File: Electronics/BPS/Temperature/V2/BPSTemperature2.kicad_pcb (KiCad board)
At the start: 2 copper layers, 75 x 65 mm, 80 parts, among them J1 Conn_02x10_Counter_Clockwise, J2 Logic Analyzer, J3 Conn_02x06_Counter_Clockwise, J4 Conn_02x06_Counter_Clockwise, SW1 SW_DIP_x06, U1 LTC2983

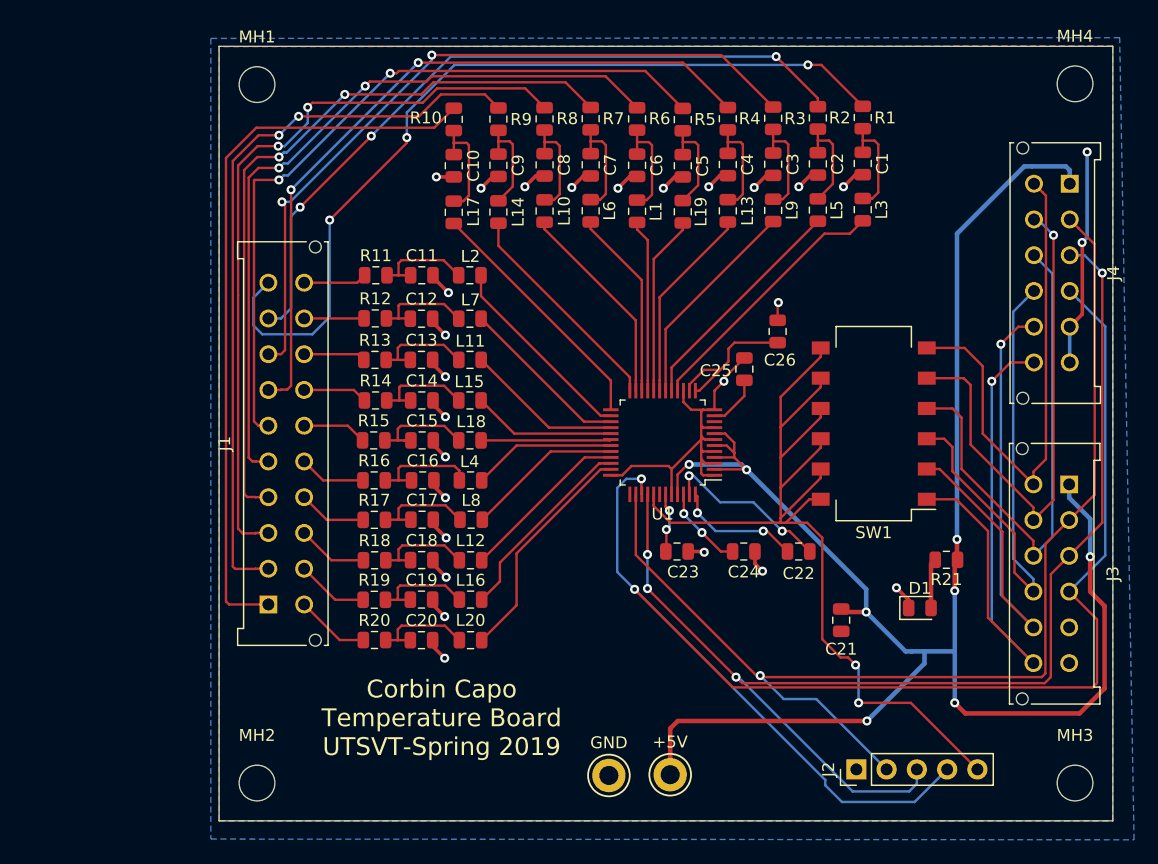
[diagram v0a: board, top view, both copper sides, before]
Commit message: Rotated components of Temperature Board for BPS
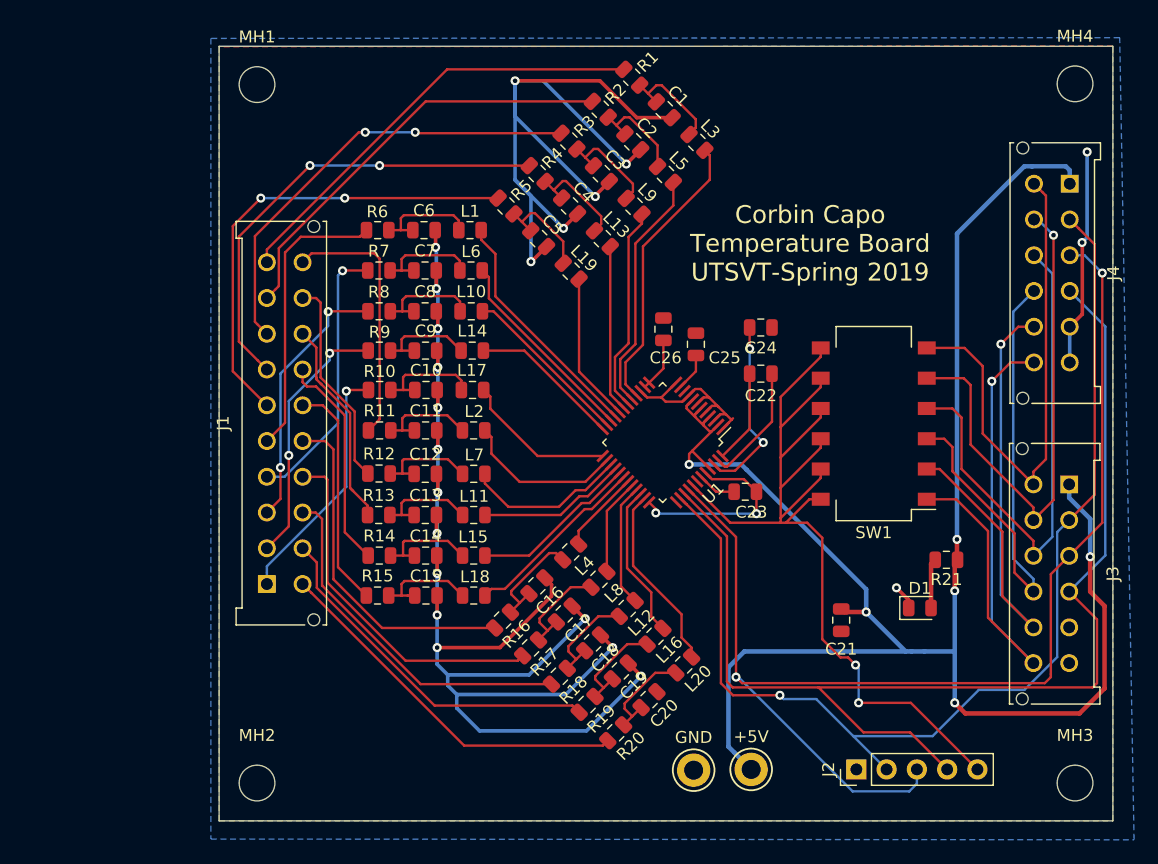
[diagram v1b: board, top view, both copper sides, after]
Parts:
- moved R6 23.7 mm to (73.3, 85.4), turned to 0 degrees
- moved R10 23.5 mm to (73.5, 98.8), turned to 0 degrees
- moved R7 21.9 mm to (73.4, 88.8), turned to 0 degrees
- moved R9 21.8 mm to (73.4, 95.5), turned to 0 degrees
- moved R20 21.7 mm to (93.3, 127.6), turned to 45 degrees
- moved R8 21.3 mm to (73.4, 92.2), turned to 0 degrees
- moved R19 19.9 mm to (90.9, 125.2), turned to 45 degrees
- moved C20 19.7 mm to (96.1, 124.8), turned to 45 degrees
- moved R1 19.7 mm to (94.6, 72.6), turned to 315 degrees
- moved C10 19.0 mm to (77.4, 98.8), turned to 0 degrees
- moved C24 18.9 mm to (105.5, 93.6)
- moved C6 18.7 mm to (77.2, 85.4), turned to 0 degrees
- moved R18 18.3 mm to (88.6, 122.9), turned to 45 degrees
- moved R2 18.3 mm to (92.0, 75.3), turned to 315 degrees
- moved L20 18.0 mm to (99.0, 121.9), turned to 225 degrees
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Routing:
- net GND: track 95.2 -> 239.7 mm, vias 27 -> 24
- net /CH10_LPF: track 61.7 -> 20.9 mm, vias 0 -> 1
- net /CH8_LPF: track 63.0 -> 22.3 mm
- net /CH9_LPF: track 62.2 -> 21.9 mm
- net /CH7_LPF: track 62.3 -> 22.9 mm, vias 2 -> 1
- net /CH6_LPF: track 62.5 -> 24.1 mm, vias 2 -> 0
- net /CH1_LPF: track 72.6 -> 37.3 mm, vias 3 -> 0
- net /MISO: track 126.5 -> 98.6 mm, vias 2 -> 0
- net /CH2_LPF: track 61.9 -> 36.0 mm, vias 3 -> 0
- net /CH20_LPF: track 6.20 -> 31.4 mm
- net /CH3_LPF: track 62.5 -> 37.9 mm
- net /CH17_LPF: track 5.74 -> 30.1 mm
- net /CH18_LPF: track 5.93 -> 30.1 mm
- net /CH19_LPF: track 6.03 -> 30.2 mm
- net /CH16_LPF: track 5.60 -> 29.0 mm
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
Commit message: Modified rotated board for BPS
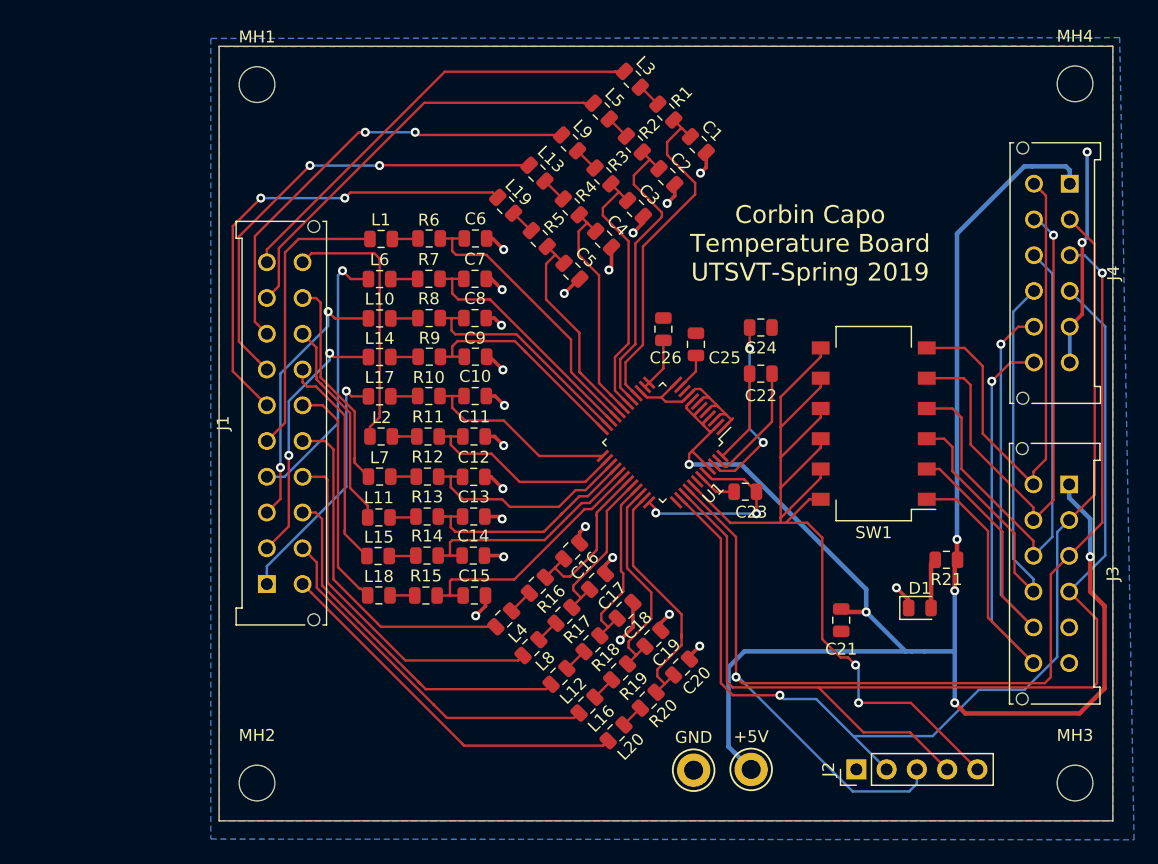
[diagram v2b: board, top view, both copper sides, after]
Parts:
- moved L16 8.12 mm to (90.9, 125.3), turned to 45 degrees
- moved L8 8.09 mm to (86.2, 120.5), turned to 45 degrees
- moved L12 8.08 mm to (88.5, 122.9), turned to 45 degrees
- moved L20 8.04 mm to (93.3, 127.6), turned to 45 degrees
- moved L15 8.02 mm to (73.3, 112.8), turned to 0 degrees
- moved L11 7.97 mm to (73.4, 109.5), turned to 0 degrees
- moved L18 7.96 mm to (73.4, 116.1), turned to 0 degrees
- moved L4 7.94 mm to (83.9, 118.0), turned to 45 degrees
- moved L7 7.90 mm to (73.5, 106.1), turned to 0 degrees
- moved L17 7.82 mm to (73.5, 99.4)
- moved L14 7.79 mm to (73.5, 96.1), turned to 0 degrees
- moved L19 7.79 mm to (84.0, 83.3)
- moved L2 7.78 mm to (73.6, 102.7), turned to 0 degrees
- moved L13 7.77 mm to (86.7, 80.6)
- moved L10 7.71 mm to (73.5, 92.8), turned to 0 degrees
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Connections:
- L1 pad 1: Net-(L1-Pad1) -> /CH6_LPF
- L1 pad 2: Net-(C6-Pad1) -> Net-(L1-Pad2)
- L10 pad 1: Net-(L10-Pad1) -> /CH8_LPF
- L10 pad 2: Net-(C8-Pad1) -> Net-(L10-Pad2)
- L11 pad 1: Net-(L11-Pad1) -> /CH13_LPF
- L11 pad 2: Net-(C13-Pad1) -> Net-(L11-Pad2)
- L12 pad 1: Net-(L12-Pad1) -> /CH18_LPF
- L12 pad 2: Net-(C18-Pad1) -> Net-(L12-Pad2)
- L13 pad 2: Net-(C4-Pad1) -> /CH4_LPF
- L14 pad 1: Net-(L14-Pad1) -> /CH9_LPF
- L14 pad 2: Net-(C9-Pad1) -> Net-(L14-Pad2)
- L15 pad 1: Net-(L15-Pad1) -> /CH14_LPF
- L15 pad 2: Net-(C14-Pad1) -> Net-(L15-Pad2)
- L16 pad 1: Net-(L16-Pad1) -> /CH19_LPF
- L16 pad 2: Net-(C19-Pad1) -> Net-(L16-Pad2)
- L17 pad 2: Net-(C10-Pad1) -> /CH10_LPF
- L18 pad 1: Net-(L18-Pad1) -> /CH15_LPF
- L18 pad 2: Net-(C15-Pad1) -> Net-(L18-Pad2)
- L19 pad 2: Net-(C5-Pad1) -> /CH5_LPF
- L2 pad 1: Net-(L2-Pad1) -> /CH11_LPF
- L2 pad 2: Net-(C11-Pad1) -> Net-(L2-Pad2)
- L20 pad 1: Net-(L20-Pad1) -> /CH20_LPF
- L20 pad 2: Net-(C20-Pad1) -> Net-(L20-Pad2)
- L3 pad 2: Net-(C1-Pad1) -> /CH1_LPF
- L4 pad 1: Net-(L4-Pad1) -> /CH16_LPF
- L4 pad 2: Net-(C16-Pad1) -> Net-(L4-Pad2)
- L5 pad 2: Net-(C2-Pad1) -> /CH2_LPF
- L6 pad 1: Net-(L6-Pad1) -> /CH7_LPF
- L6 pad 2: Net-(C7-Pad1) -> Net-(L6-Pad2)
- L7 pad 1: Net-(L7-Pad1) -> /CH12_LPF
- L7 pad 2: Net-(C12-Pad1) -> Net-(L7-Pad2)
- L8 pad 1: Net-(L8-Pad1) -> /CH17_LPF
- L8 pad 2: Net-(C17-Pad1) -> Net-(L8-Pad2)
- L9 pad 2: Net-(C3-Pad1) -> /CH3_LPF
- R1 pad 1: /CH1_LPF -> Net-(L3-Pad1)
- R10 pad 1: /CH10_LPF -> Net-(L17-Pad1)
- R11 pad 1: /CH11_LPF -> Net-(L2-Pad2)
- R12 pad 1: /CH12_LPF -> Net-(L7-Pad2)
- R13 pad 1: /CH13_LPF -> Net-(L11-Pad2)
- R14 pad 1: /CH14_LPF -> Net-(L15-Pad2)
- R15 pad 1: /CH15_LPF -> Net-(L18-Pad2)
- R16 pad 1: /CH16_LPF -> Net-(L4-Pad2)
- R17 pad 1: /CH17_LPF -> Net-(L8-Pad2)
- R18 pad 1: /CH18_LPF -> Net-(L12-Pad2)
- R19 pad 1: /CH19_LPF -> Net-(L16-Pad2)
- R2 pad 1: /CH2_LPF -> Net-(L5-Pad1)
- R20 pad 1: /CH20_LPF -> Net-(L20-Pad2)
- R3 pad 1: /CH3_LPF -> Net-(L9-Pad1)
- R4 pad 1: /CH4_LPF -> Net-(L13-Pad1)
- R5 pad 1: /CH5_LPF -> Net-(L19-Pad1)
- R6 pad 1: /CH6_LPF -> Net-(L1-Pad2)
- R7 pad 1: /CH7_LPF -> Net-(L6-Pad2)
- R8 pad 1: /CH8_LPF -> Net-(L10-Pad2)
- R9 pad 1: /CH9_LPF -> Net-(L14-Pad2)
- U1 pad 16: Net-(L3-Pad1) -> Net-(C1-Pad1)
- U1 pad 17: Net-(L5-Pad1) -> Net-(C2-Pad1)
- U1 pad 18: Net-(L9-Pad1) -> Net-(C3-Pad1)
- U1 pad 19: Net-(L13-Pad1) -> Net-(C4-Pad1)
- U1 pad 20: Net-(L19-Pad1) -> Net-(C5-Pad1)
- U1 pad 21: Net-(L1-Pad1) -> Net-(C6-Pad1)
- U1 pad 22: Net-(L6-Pad1) -> Net-(C7-Pad1)
- U1 pad 23: Net-(L10-Pad1) -> Net-(C8-Pad1)
- U1 pad 24: Net-(L14-Pad1) -> Net-(C9-Pad1)
- U1 pad 25: Net-(L17-Pad1) -> Net-(C10-Pad1)
- U1 pad 26: Net-(L2-Pad1) -> Net-(C11-Pad1)
- U1 pad 27: Net-(L7-Pad1) -> Net-(C12-Pad1)
- U1 pad 28: Net-(L11-Pad1) -> Net-(C13-Pad1)
- U1 pad 29: Net-(L15-Pad1) -> Net-(C14-Pad1)
- U1 pad 30: Net-(L18-Pad1) -> Net-(C15-Pad1)
- U1 pad 31: Net-(L4-Pad1) -> Net-(C16-Pad1)
- U1 pad 32: Net-(L8-Pad1) -> Net-(C17-Pad1)
- U1 pad 33: Net-(L12-Pad1) -> Net-(C18-Pad1)
- U1 pad 34: Net-(L16-Pad1) -> Net-(C19-Pad1)
- U1 pad 35: Net-(L20-Pad1) -> Net-(C20-Pad1)
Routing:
- net GND: track 239.7 -> 90.1 mm, vias 24 -> 25
- net Net-(L3-Pad1): track 24.0 -> 2.07 mm
- net Net-(L1-Pad1): track 20.3 -> 0.00 mm
- net Net-(C1-Pad1): track 8.97 -> 28.7 mm
- net Net-(L5-Pad1): track 20.5 -> 2.04 mm
- net Net-(L6-Pad1): track 17.1 -> 0.00 mm
- net Net-(C2-Pad1): track 8.47 -> 25.5 mm
- net Net-(L18-Pad1): track 15.8 -> 0.00 mm
- net Net-(L20-Pad1): track 15.8 -> 0.00 mm
- net Net-(L9-Pad1): track 17.3 -> 2.08 mm
- net Net-(C6-Pad1): track 8.97 -> 24.1 mm
- net Net-(L10-Pad1): track 14.4 -> 0.00 mm
- net Net-(L15-Pad1): track 14.2 -> 0.00 mm
- net Net-(L7-Pad1): track 13.7 -> 0.00 mm
- net Net-(L2-Pad1): track 13.6 -> 0.00 mm
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
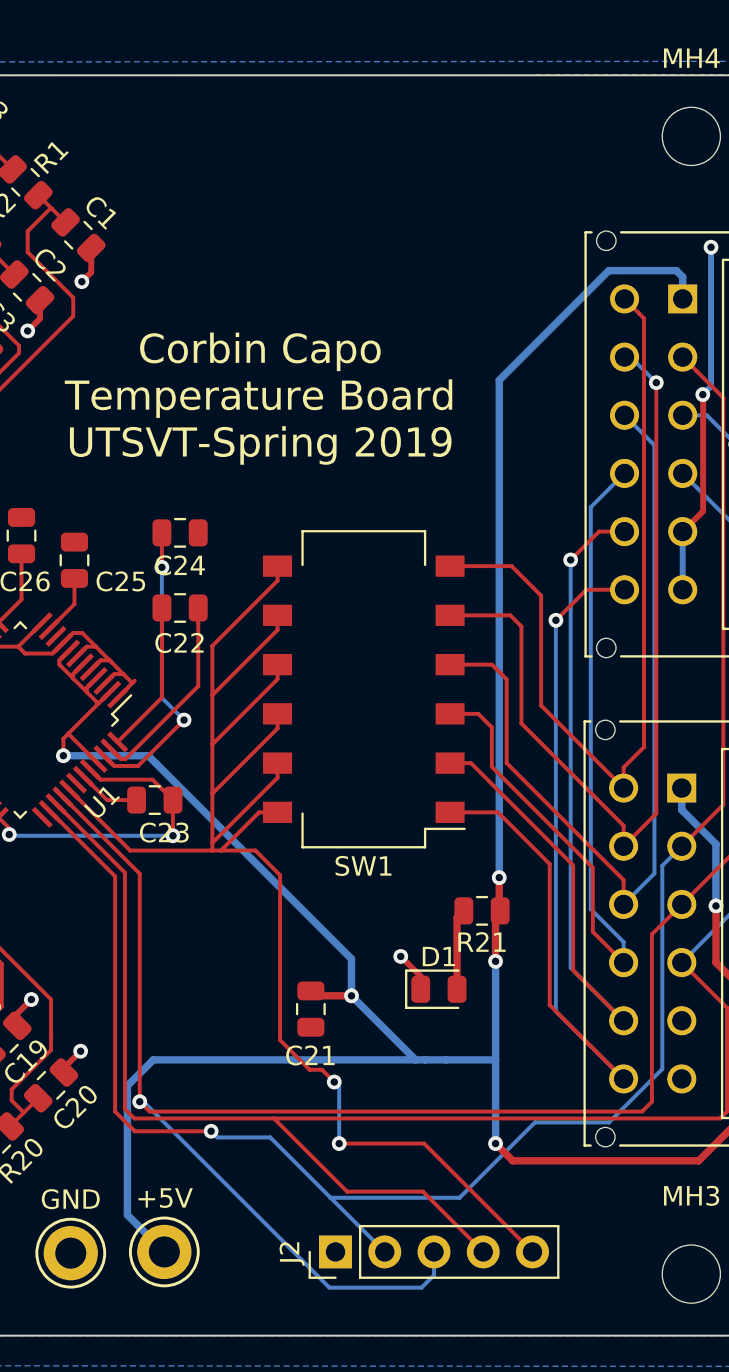
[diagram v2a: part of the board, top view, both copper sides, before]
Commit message: Added connector to temerature board for BPS
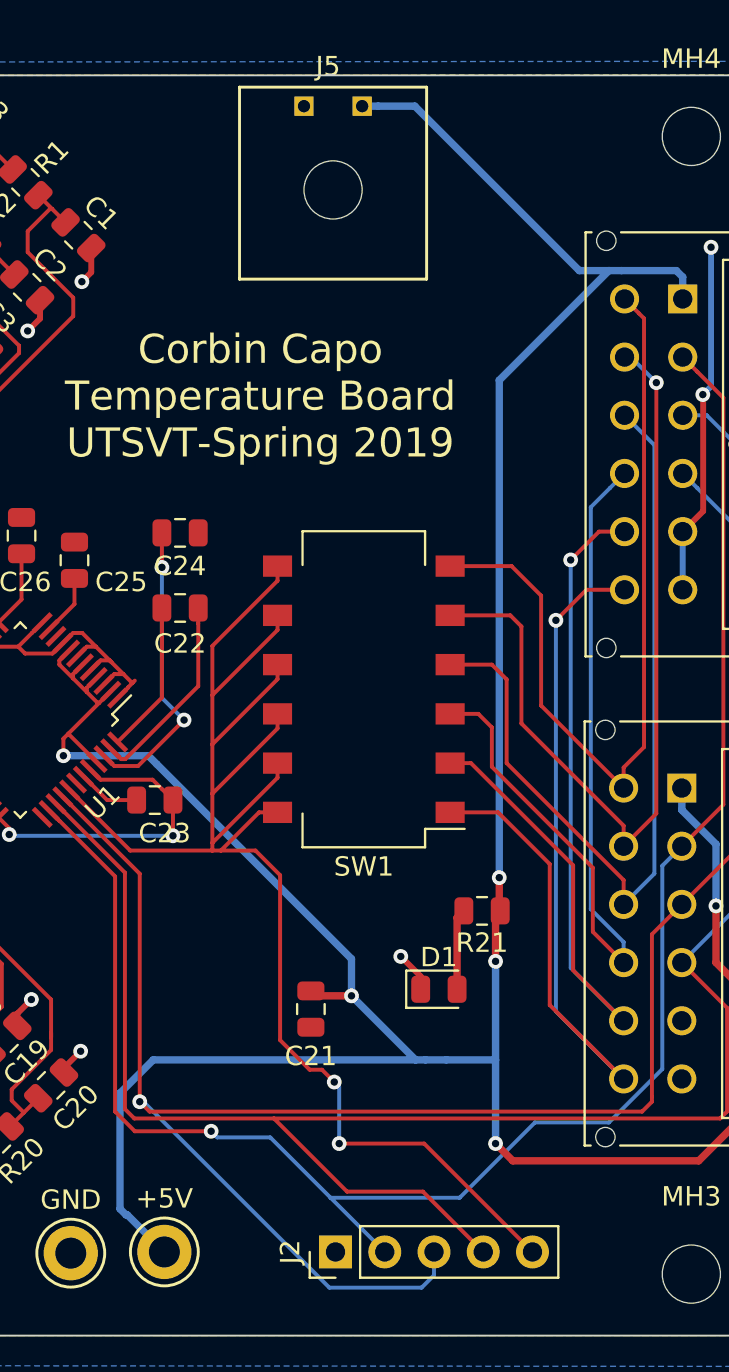
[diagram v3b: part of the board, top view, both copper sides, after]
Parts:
- added J5: Conn_01x02, UTSVT_Connectors:43650-0202_01x02_Microfit 3.0_horizontal, F.Cu at (118.2, 70.6)
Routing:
- net +5V: track 153.9 -> 170.5 mm

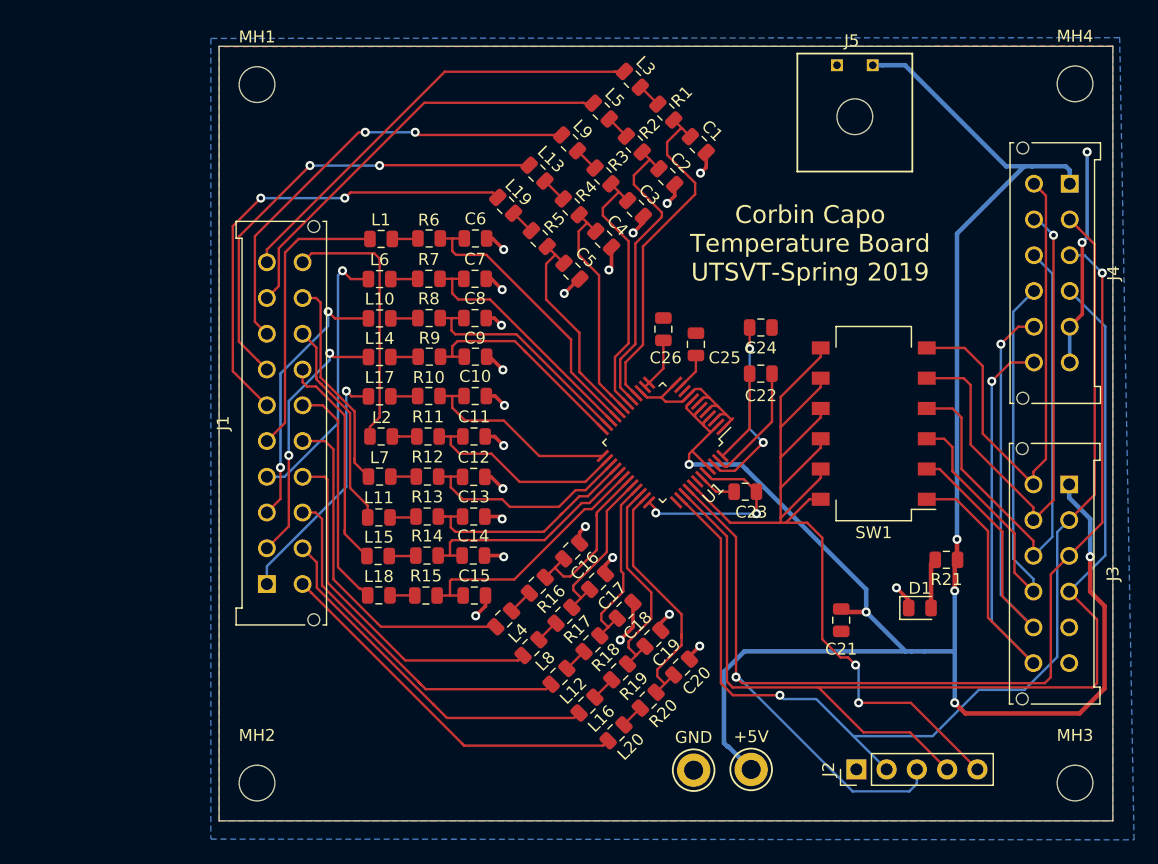
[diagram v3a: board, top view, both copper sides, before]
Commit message: Redid pin layout for connector to filters
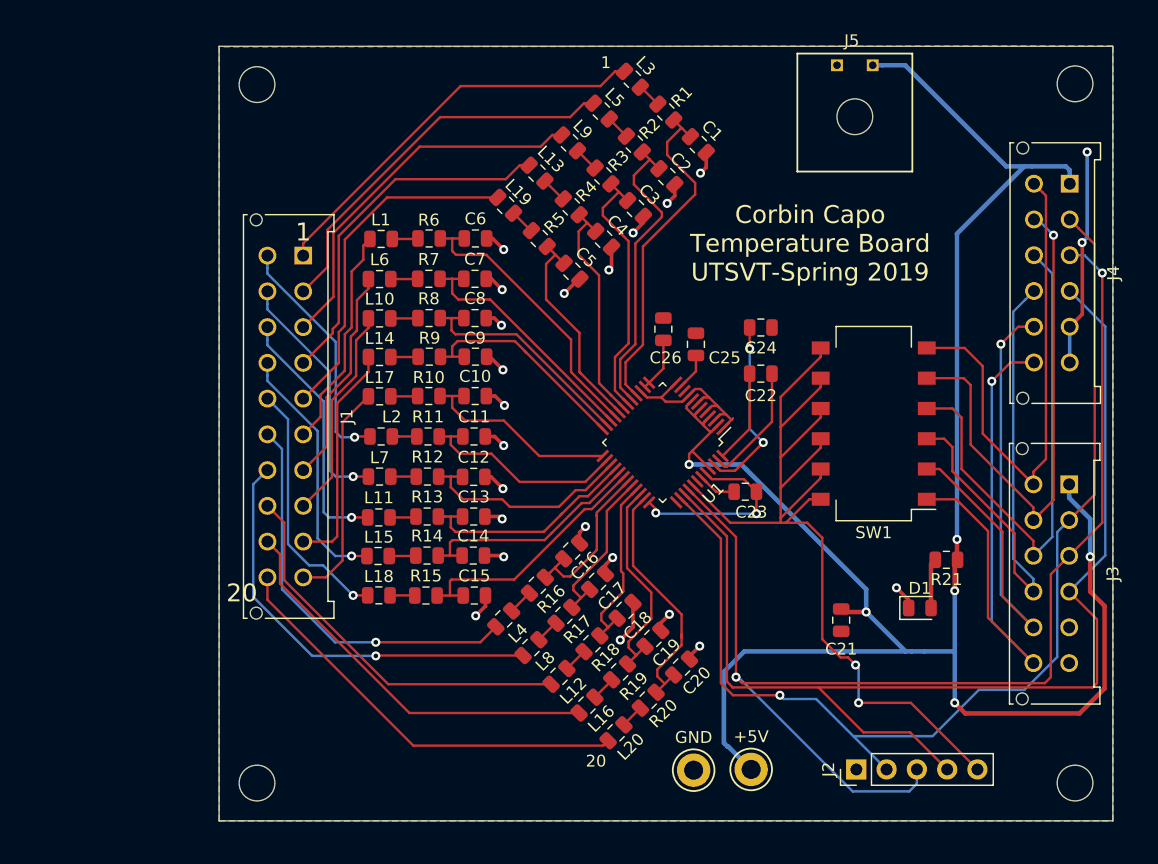
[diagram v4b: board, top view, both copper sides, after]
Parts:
- moved J1 27.7 mm to (67.1, 87.6), turned to 270 degrees
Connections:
- J1 pad 1: /CH10_LPF -> /CH1_LPF
- J1 pad 10: /CH1_LPF -> /CH10_LPF
- J1 pad 11: /CH20_LPF -> /CH11_LPF
- J1 pad 12: /CH19_LPF -> /CH12_LPF
- J1 pad 13: /CH18_LPF -> /CH13_LPF
- J1 pad 14: /CH17_LPF -> /CH14_LPF
- J1 pad 15: /CH16_LPF -> /CH15_LPF
- J1 pad 16: /CH15_LPF -> /CH16_LPF
- J1 pad 17: /CH14_LPF -> /CH17_LPF
- J1 pad 18: /CH13_LPF -> /CH18_LPF
- J1 pad 19: /CH12_LPF -> /CH19_LPF
- J1 pad 2: /CH9_LPF -> /CH2_LPF
- J1 pad 20: /CH11_LPF -> /CH20_LPF
- J1 pad 3: /CH8_LPF -> /CH3_LPF
- J1 pad 4: /CH7_LPF -> /CH4_LPF
- J1 pad 5: /CH6_LPF -> /CH5_LPF
- J1 pad 6: /CH5_LPF -> /CH6_LPF
- J1 pad 7: /CH4_LPF -> /CH7_LPF
- J1 pad 8: /CH3_LPF -> /CH8_LPF
- J1 pad 9: /CH2_LPF -> /CH9_LPF
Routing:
- net /CH5_LPF: track 39.8 -> 29.1 mm, vias 2 -> 0
- net /CH4_LPF: track 39.0 -> 30.3 mm, vias 2 -> 0
- net /CH3_LPF: track 38.2 -> 31.5 mm, vias 2 -> 0
- net /CH17_LPF: track 30.1 -> 35.8 mm, vias 0 -> 1
- net /CH6_LPF: track 24.0 -> 18.7 mm
- net /CH7_LPF: track 23.3 -> 18.3 mm, vias 1 -> 0
- net /CH16_LPF: track 29.1 -> 33.8 mm, vias 0 -> 1
- net /CH8_LPF: track 22.6 -> 18.0 mm, vias 2 -> 0
- net /CH20_LPF: track 31.7 -> 35.7 mm
- net /CH13_LPF: track 17.8 -> 21.4 mm, vias 0 -> 1
- net /CH2_LPF: track 36.1 -> 32.7 mm
- net /CH1_LPF: track 37.3 -> 34.0 mm
- net /CH9_LPF: track 22.2 -> 19.2 mm, vias 2 -> 0
- net /CH19_LPF: track 30.7 -> 33.6 mm
- net /CH14_LPF: track 18.5 -> 21.2 mm, vias 0 -> 1
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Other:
- board text added: "1"
- board text added: "20"
